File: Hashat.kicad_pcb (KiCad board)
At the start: 2 copper layers, 65 x 56.5 mm, 114 parts, among them CN1 HF1004E, IC1 BM1397_mode1, J1 Raspberry_Pi_2_3, J3 Conn_01x05, Q1 CSD17311Q5, Q2 CSD17311Q5, U10 DS4432U+, U2 LN1134A182MR-G, U3 SN74LVC1T45DBVR, U4 SGM2036-ADJYN5G/TR, U5 SN74LVC1T45DBVR, U6 SN74LVC1T45DBVR, U7 EMC2101-R, U8 SN74LVC1T45DBVR, U9 TPS40305, X1 OT322525MJBA4SL

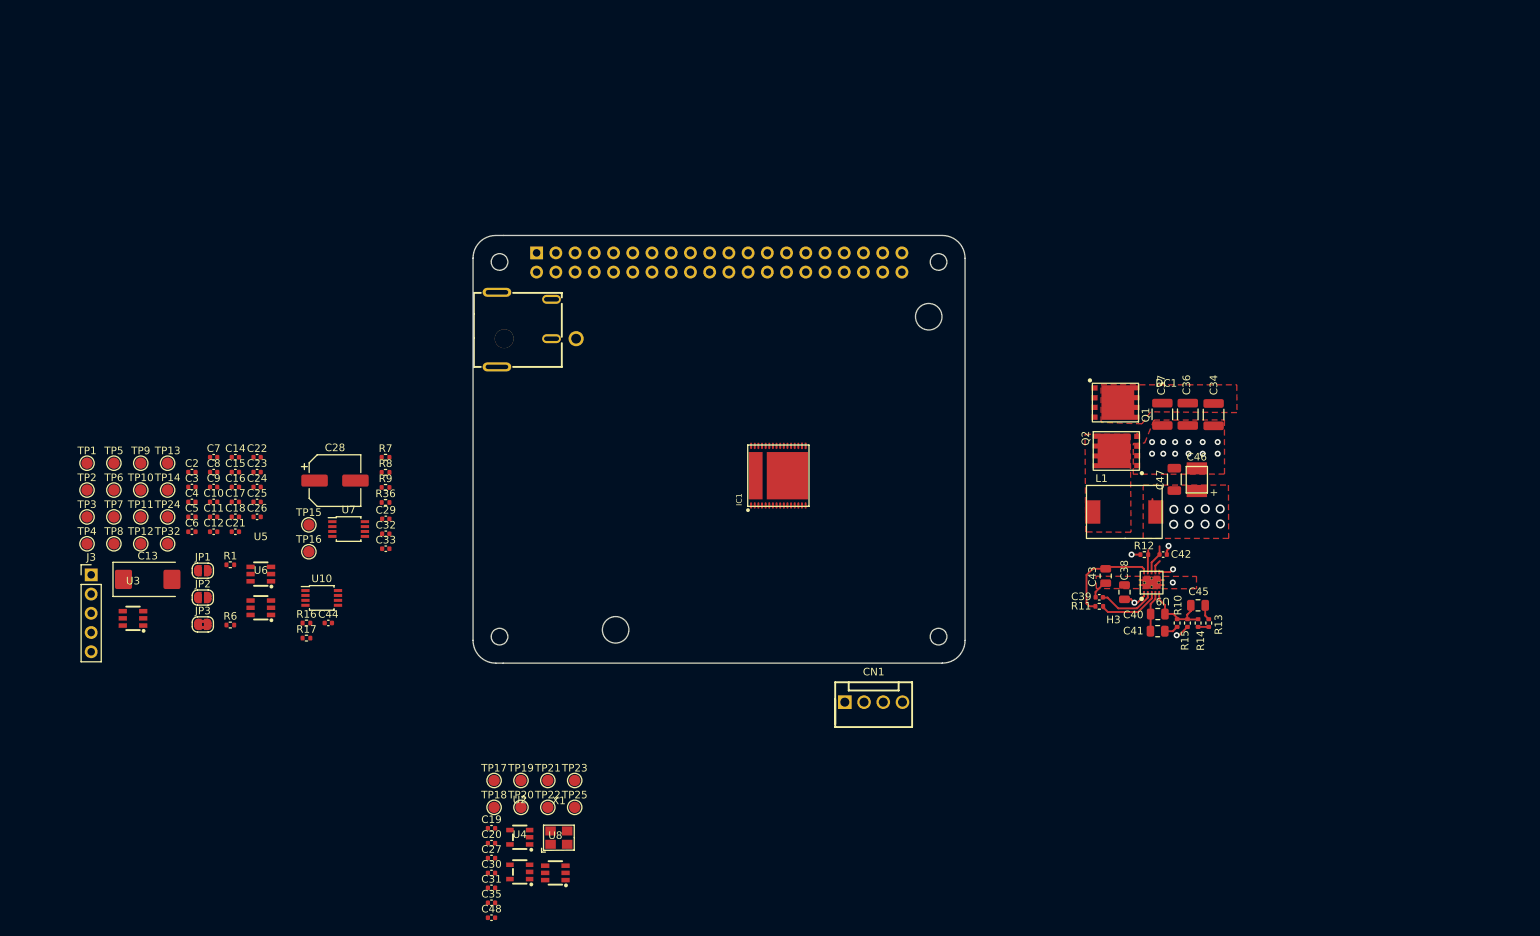
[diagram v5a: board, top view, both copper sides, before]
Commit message: adding 3D models. lots of placement. a little routing started
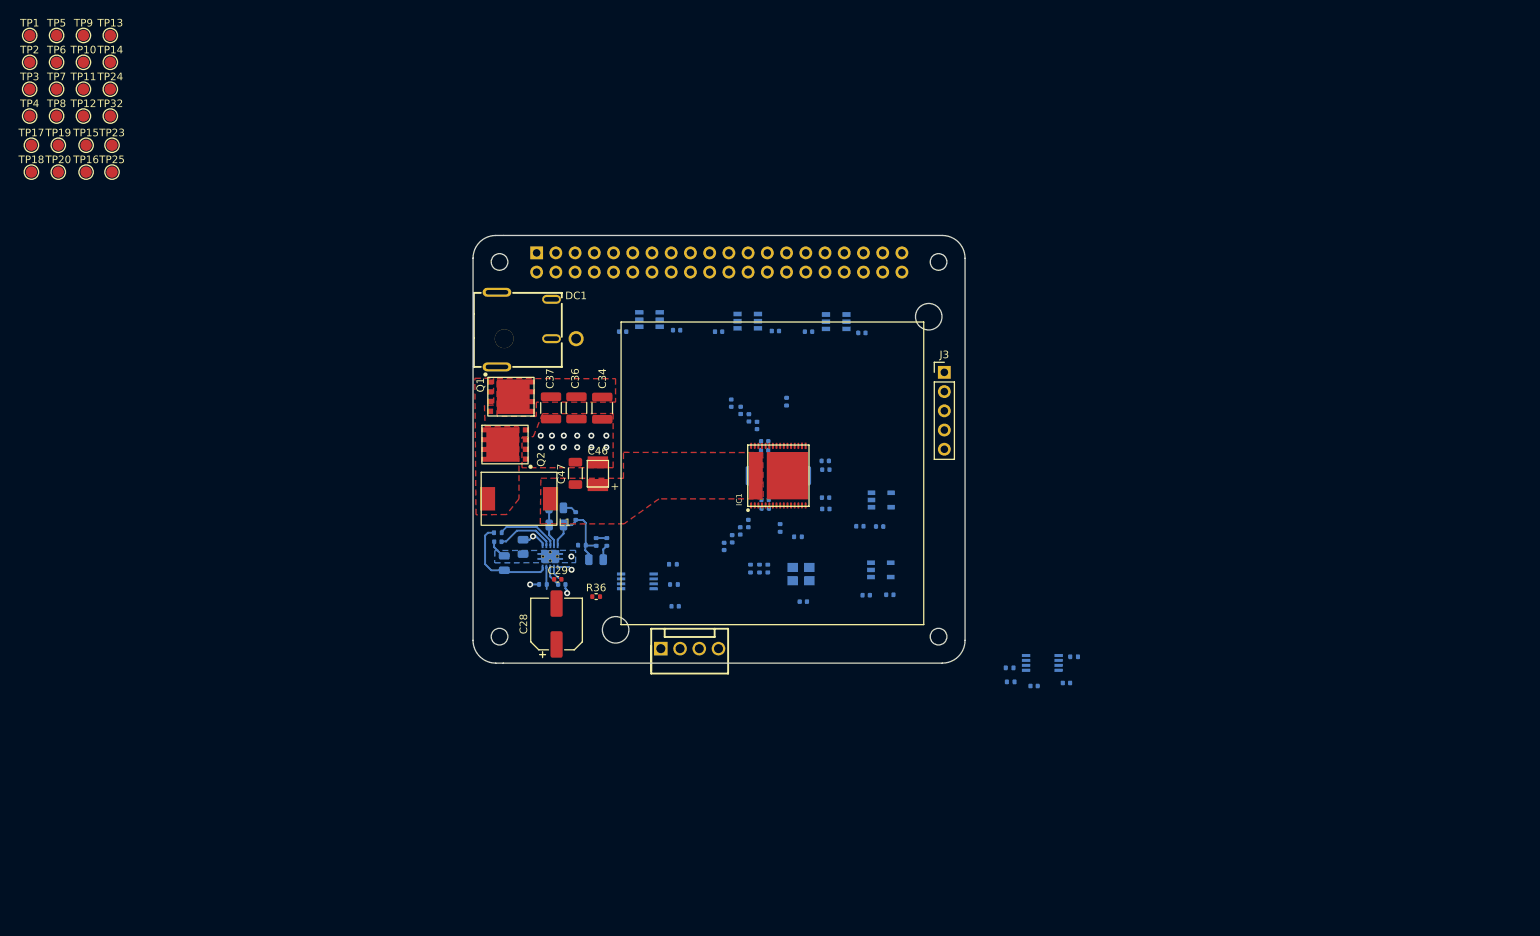
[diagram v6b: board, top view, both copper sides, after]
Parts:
- removed C27, C30: 311-3342-1-ND, Capacitor_SMD:C_0402_1005Metric
- removed JP1, JP2: SolderJumper_2_Open, Jumper:SolderJumper-2_P1.3mm_Open_RoundedPad1.0x1.5mm
- removed JP3: SolderJumper_2_Bridged, Jumper:SolderJumper-2_P1.3mm_Bridged2Bar_RoundedPad1.0x1.5mm
- removed TP21, TP22: TestPoint, TestPoint:TestPoint_Pad_D1.5mm
- removed U6: SN74LVC1T45DBVR, lcsc:SOT-23-6_L2.9-W1.6-P0.95-LS2.8-BR
- added R2: 1k, Resistor_SMD:R_0402_1005Metric, B.Cu at (119.9, 95.3)
- added R3: 0, Resistor_SMD:R_0402_1005Metric, B.Cu at (113.7, 99.5)
- added R4: 0, Resistor_SMD:R_0402_1005Metric, B.Cu at (114.8, 99.5)
- added R5: 0, Resistor_SMD:R_0402_1005Metric, B.Cu at (115.9, 99.5)
- C10, C11, C12, C13, C14, C15, C16, C17, C18, C19, C2, C20, C21, C22, C23, C24, C25, C26, C3, C31, C32, C33, C35, C38, C39, C4, C40, C41, C42, C43, C44, C45, C48, C5, C6, C7, C8, C9, R1, R10, R11, R12, R13, R14, R15, R16, R17, R6, R7, R8, R9, U10, U2, U3, U4, U5, U7, U8, U9, X1: moved to B.Cu
- moved J3 115.8 mm to (139.3, 73.6)
- moved TP17 103.8 mm to (18.7, 43.6)
- moved TP18 103.8 mm to (18.7, 47.1)
- moved TP19 103.8 mm to (22.2, 43.6)
- moved TP20 103.8 mm to (22.2, 47.1)
- moved TP23 103.8 mm to (29.3, 43.6)
- moved TP25 103.8 mm to (29.3, 47.1)
- moved R9 93.7 mm to (156.4, 111.2), turned to 180 degrees
- moved U7 93.3 mm to (152.2, 112.0), turned to 180 degrees
- moved C33 91.7 mm to (155.4, 114.6), turned to 180 degrees
- moved U3 90.2 mm to (113.3, 66.8), turned to 180 degrees
- moved C35 89.8 mm to (128.4, 68.4), turned to 180 degrees
- moved C32 88.0 mm to (151.1, 115.0), turned to 180 degrees
- moved R7 87.8 mm to (148.0, 114.5), turned to 180 degrees
- moved R8 86.4 mm to (147.9, 112.6), turned to 180 degrees
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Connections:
- net /BM1397/BI renamed Net-(IC1-BI)
- J1 pad 10: /RPi/RO -> /BM1397/BM_RO
- J1 pad 11: /RPi/RST -> /BM1397/BM_RST
- J1 pad 36: /RPi/BI -> unconnected-(J1-GPIO16-Pad36)
- J1 pad 8: /RPi/CI -> /BM1397/BM_CI
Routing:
- net /Power/OUT0: track 9.84 -> 12.9 mm
- net /BM1397/VDD: track 3.36 -> 1.47 mm
- net GND: track 5.60 -> 3.72 mm, vias 15 -> 14
- net /Power/SW: track 3.85 -> 2.74 mm
- net (no net): vias 8 -> 0
- added copper zone on B.Cu, net GND

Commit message: more routing
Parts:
- removed CN1: HF1004E, lcsc:CONN-TH_4P-P2.54_A2510S-4P
- added J2: Conn_01x04, Connector_PinHeader_2.54mm:PinHeader_1x04_P2.54mm_Vertical, F.Cu at (139.3, 95.8)
- C28, C29, R36: moved to B.Cu
- moved C28 45.6 mm to (132.7, 97.6)
- moved C29 44.3 mm to (132.4, 104.8), turned to 180 degrees
- moved R36 42.2 mm to (135.4, 104.8), turned to 180 degrees
- moved C33 35.5 mm to (123.0, 100.2), turned to -90 degrees
- moved C20 29.7 mm to (130.8, 73.4), turned to 90 degrees
- moved C19 29.6 mm to (133.4, 73.4), turned to 90 degrees
- moved R9 29.2 mm to (128.3, 103.3), turned to -90 degrees
- moved C32 29.0 mm to (125.7, 101.1), turned to 0 degrees
- moved U7 27.3 mm to (125.8, 105.1), turned to -90 degrees
- moved R7 26.5 mm to (126.3, 99.3), turned to 90 degrees
- moved R8 26.3 mm to (125.2, 99.3), turned to -90 degrees
- moved U2 23.2 mm to (132.2, 76.5), turned to 0 degrees
- moved C22 12.5 mm to (133.3, 81.7), turned to 90 degrees
- moved C24 12.5 mm to (130.7, 81.7), turned to 90 degrees
- moved R16 10.7 mm to (92.7, 100.1)
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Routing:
- net /BM1397/CI: track 0.00 -> 109.7 mm, vias 0 -> 3
- net /5V: track 3.50 -> 112.7 mm, vias 1 -> 3
- net /BM1397/RO: track 0.00 -> 102.4 mm, vias 0 -> 3
- net /BM1397/RST_N: track 0.00 -> 91.4 mm, vias 0 -> 1
- net /Fan/SDA: track 0.00 -> 57.6 mm
- net /Fan/SCL: track 0.00 -> 57.6 mm
- net /BM1397/0V8: track 0.00 -> 43.7 mm, vias 0 -> 3
- net Net-(Q1-G): track 1.69 -> 44.1 mm, vias 0 -> 1
- net /BM1397/1V8: track 0.00 -> 41.9 mm, vias 0 -> 4
- net Net-(Q2-G): track 2.92 -> 35.9 mm, vias 0 -> 1
- net /BM1397/BM_RST: track 0.00 -> 32.5 mm
- net /BM1397/TEMP_P: track 0.00 -> 30.7 mm, vias 0 -> 1
- net /BM1397/TEMP_N: track 0.00 -> 28.4 mm, vias 0 -> 1
- net /BM1397/BM_RO: track 0.00 -> 24.1 mm, vias 0 -> 1
- net /Fan/FAN_TACH: track 0.00 -> 17.3 mm
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- added copper zone on In2.Cu, net /3V3
- added copper zone on B.Cu, net /BM1397/VDD
- added copper zone on In1.Cu, net GND
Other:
- copper layers 2 -> 4

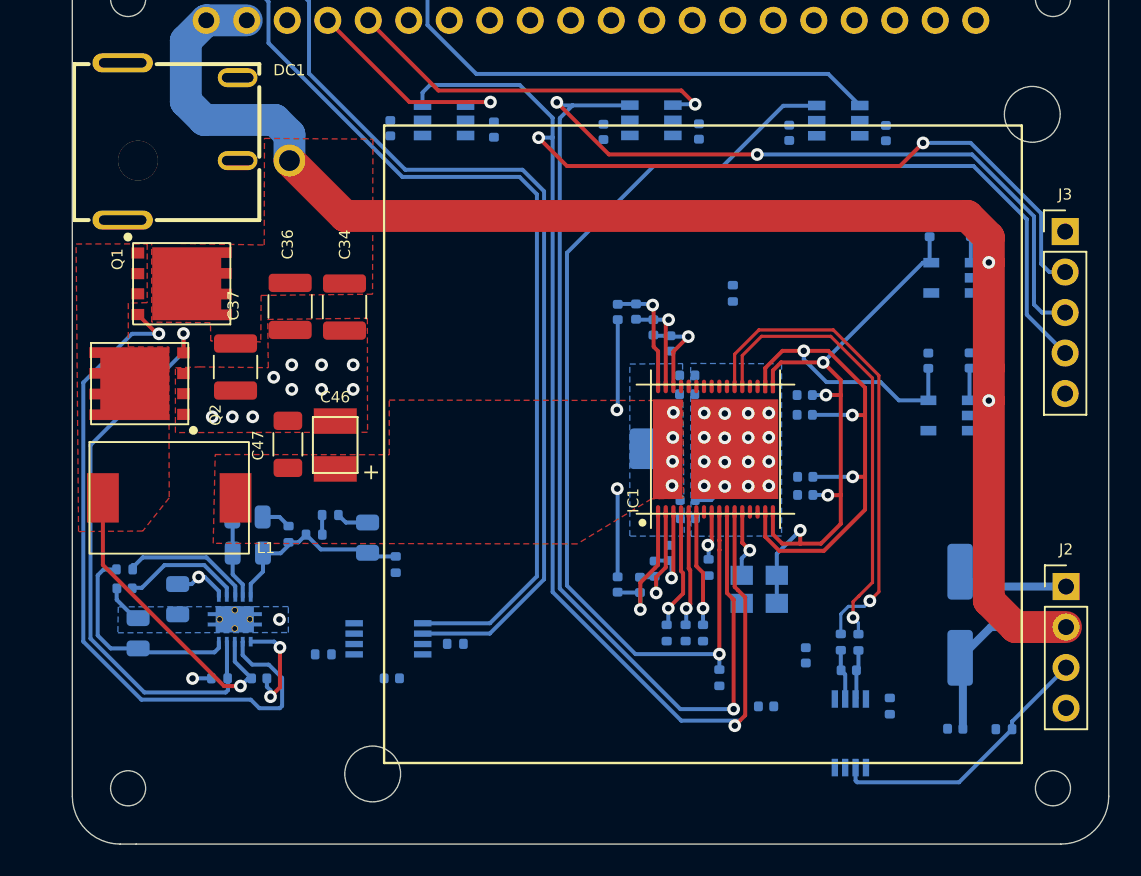
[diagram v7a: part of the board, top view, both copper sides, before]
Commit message: pretty much all the signals are routed
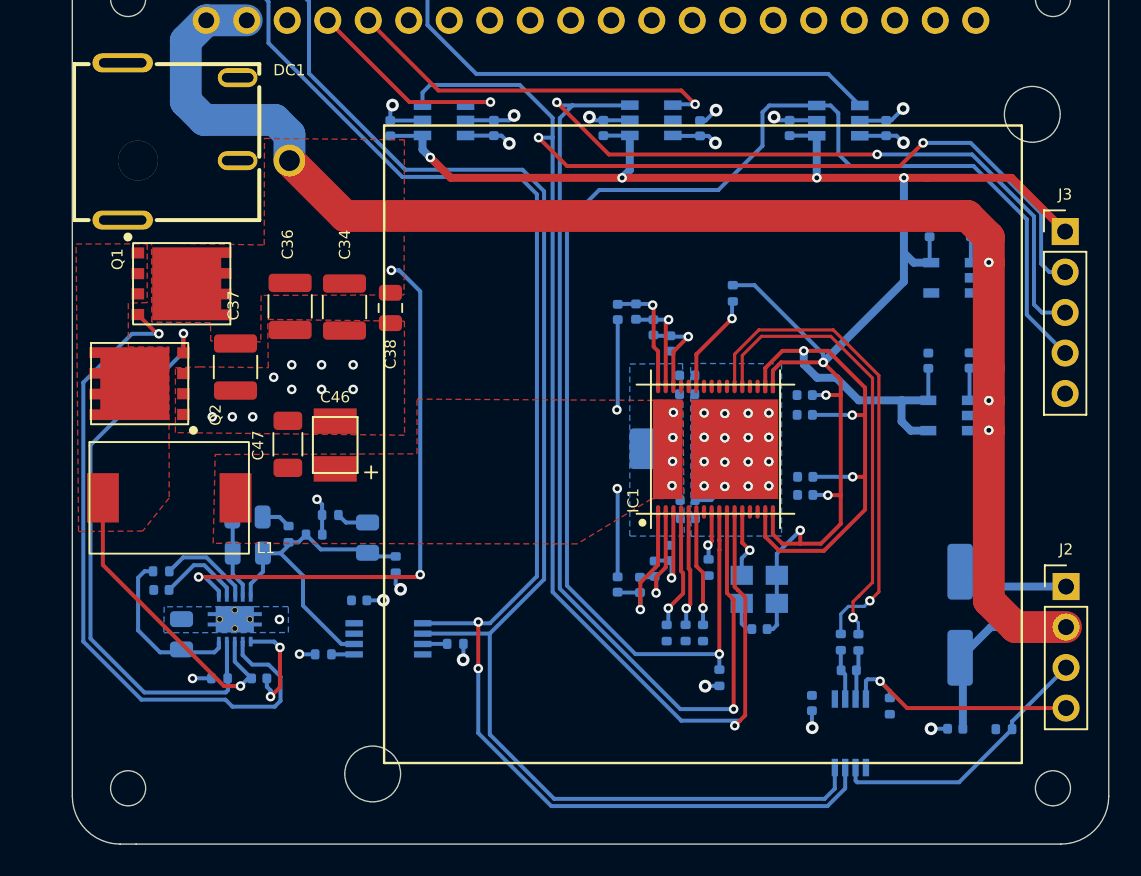
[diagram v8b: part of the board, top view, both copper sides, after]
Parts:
- C38: moved to F.Cu
- moved C38 22.6 mm to (97.0, 78.4)
- moved C44 5.30 mm to (95.0, 96.7)
- moved C48 4.86 mm to (120.1, 98.5)
- moved C33 3.02 mm to (123.4, 103.2)
- moved C43 2.72 mm to (83.8, 98.8)
- moved C39 2.31 mm to (82.6, 96.1)
- moved R11 2.30 mm to (82.6, 94.9)
- moved C35 0.32 mm to (128.0, 67.1)
- moved C31 0.30 mm to (122.0, 67.1)
- moved C21 0.25 mm to (110.3, 67.1)
- moved C26 0.22 mm to (116.4, 67.1)
- moved C25 0.10 mm to (103.4, 67.1)
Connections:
- C25 pad 1: /BM1397/3V3 -> /3V3
- C26 pad 1: /BM1397/3V3 -> /3V3
- C35 pad 1: /BM1397/3V3 -> /3V3
- U3 pad 6: /BM1397/3V3 -> /3V3
- U5 pad 6: /BM1397/3V3 -> /3V3
- U8 pad 6: /BM1397/3V3 -> /3V3
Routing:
- net /BM1397/1V8: track 41.9 -> 112.5 mm, vias 4 -> 8
- net /5V: track 112.7 -> 146.5 mm, vias 3 -> 6
- net /Fan/SDA: track 57.6 -> 91.3 mm, vias 0 -> 2
- net /Fan/SCL: track 57.6 -> 88.8 mm
- net GND: track 13.0 -> 35.6 mm, vias 28 -> 41
- net /Fan/FAN_PWM: track 0.00 -> 15.8 mm, vias 0 -> 1
- net /3V3: track 0.00 -> 8.74 mm, vias 0 -> 3
- net /Power/OUT0: track 12.6 -> 20.7 mm
- net Net-(IC1-RI): track 0.00 -> 6.28 mm, vias 0 -> 1
- net /BM1397/0V8: track 43.7 -> 47.2 mm
- net Net-(U9-BP): track 13.6 -> 10.5 mm
- net /Power/PGOOD: track 8.53 -> 5.92 mm
- net Net-(U9-SS): track 7.78 -> 5.43 mm
- net Net-(U10-FS1): track 0.00 -> 1.54 mm
- net Net-(U10-FS0): track 0.00 -> 1.43 mm
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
